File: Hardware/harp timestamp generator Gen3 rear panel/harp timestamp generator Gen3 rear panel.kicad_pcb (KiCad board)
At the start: 2 copper layers, 133 x 35 mm, 7 parts

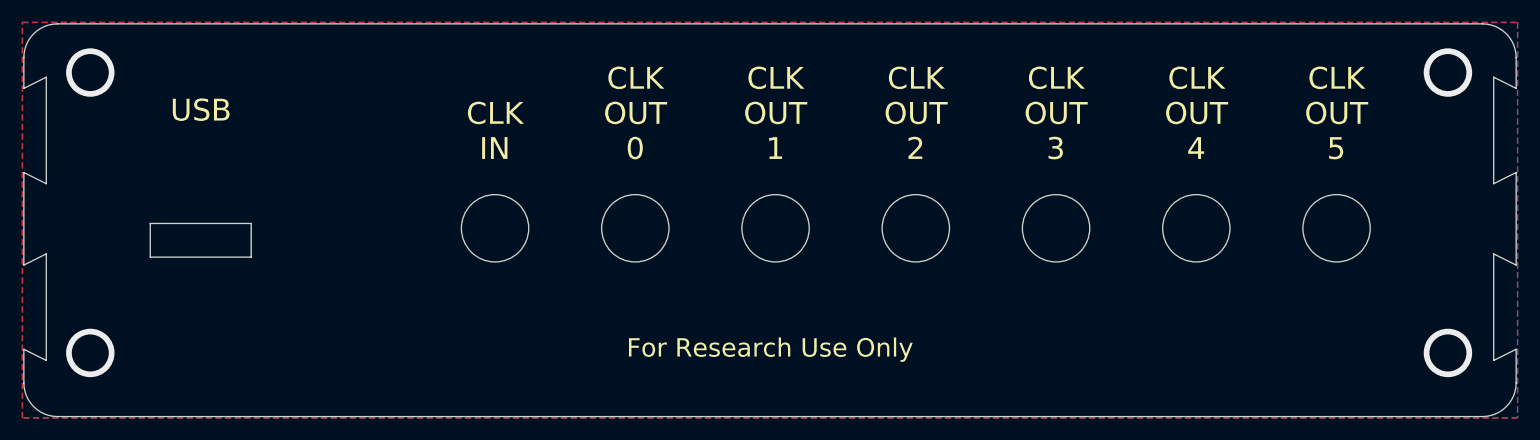
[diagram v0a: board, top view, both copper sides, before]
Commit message: review após 1ª produção de placas teste
> harp timestamp generator Gen3
  . mudança da case de Q2
  . mudança de ligação em 'Button0'

> harp timestamp generator Gen3 front panel
  . acerto no recorte da ficha IDC e interruptor bateria
  . modificação de setup no logo 'harp'

> harp timestamp generator Gen3 rear panel
  . acerto no recorte de ficha USB
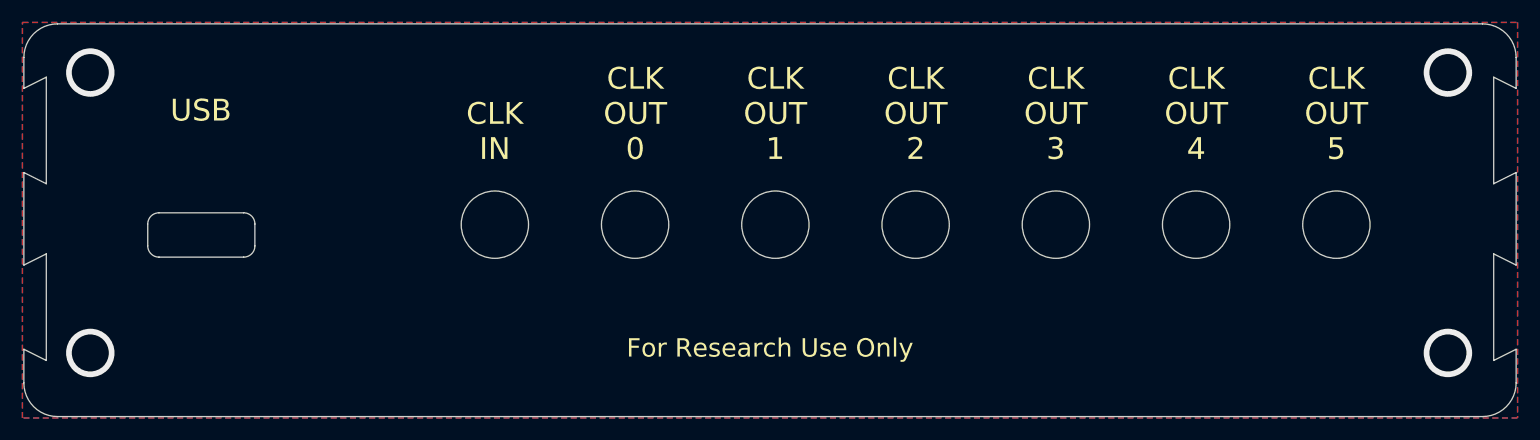
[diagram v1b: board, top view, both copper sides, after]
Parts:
- added REF**: Fiducial_Cross_1.5mm_Mask2mm, Fiducial:Fiducial_Cross_1.5mm_Mask2mm, F.Cu at (145.6, 109.0)
- moved UNK_HOLE_1 0.32 mm to (136.5, 105.4)
- moved UNK_HOLE_2 0.32 mm to (149.0, 105.4)
- moved UNK_HOLE_3 0.32 mm to (161.5, 105.4)
- moved UNK_HOLE_4 0.32 mm to (174.0, 105.4)
- moved UNK_HOLE_5 0.32 mm to (186.5, 105.4)
- moved UNK_HOLE_6 0.32 mm to (199.0, 105.4)
- moved UNK_HOLE_0 0.32 mm to (124.0, 105.4)
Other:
- outline, holes or cut-outs redrawn
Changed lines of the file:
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@@
 	(footprint "dummyfp6"
 		(layer "F.Cu")
-		(at 198.9975 105.7236)
+		(at 198.98 105.4)
 		(property "Reference" "UNK_HOLE_6"
 			(at 0 0 0)
@@
 	(footprint "dummyfp1"
 		(layer "F.Cu")
-		(at 136.4975 105.7236)
+		(at 136.48 105.4)
 		(property "Reference" "UNK_HOLE_1"
 			(at 0 0 0)
@@
 		(embedded_fonts no)
 	)
+	(footprint "Fiducial:Fiducial_Cross_1.5mm_Mask2mm"
+		(layer "F.Cu")
+		(at 145.6 109.05)
+		(descr "Fiducial, cross variant, 1.5mm bare copper, 2mm soldermask opening")
+		(tags "fiducial")
+		(property "Reference" "REF**"
+			(at 0 -1.95 0)
+			(layer "F.SilkS")
+			(hide yes)
+			(effects
+				(font
+					(size 1 1)
+					(thickness 0.15)
+				)
+			)
+		)
+		(property "Value" "Fiducial_Cross_1.5mm_Mask2mm"
+			(at 0 1.95 0)
+			(layer "F.Fab")
+			(hide yes)
+			(effects
+				(font
+					(size 1 1)
+					(thickness 0.15)
+				)
+			)
+		)
+		(property "Datasheet" ""
+			(at 0 0 0)
+			(layer "F.Fab")
+			(hide yes)
+			(effects
+				(font
+					(size 1.27 1.27)
+				)
+			)
+		)
+		(property "Description" ""
+			(at 0 0 0)
+			(layer "F.Fab")
+			(hide yes)
+			(effects
+				(font
+					(size 1.27 1.27)
+				)
+			)
+		)
+		(property "KiLib_Generator" "fiducial"
+			(at 0 0 0)
+			(layer "F.SilkS")
+			(hide yes)
+			(effects
+				(font
+					(size 1 1)
+					(thickness 0.15)
+				)
+			)
+		)
+		(attr smd board_only exclude_from_pos_files exclude_from_bom dnp)
+		(duplicate_pad_numbers_are_jumpers no)
+		(fp_circle
+			(center 0 0)
+			(end 1.25 0)
+			(stroke
+				(width 0.05)
+				(type solid)
+			)
+			(fill no)
+			(layer "F.CrtYd")
+		)
+		(embedded_fonts no)
+		(model "${KIPRJMOD}/harp timestamp generator.step"
+			(offset
+				(xyz 3 -0.75 -41.55)
+			)
+			(scale
+				(xyz 1 1 1)
+			)
+			(rotate
+				(xyz 90 -180 -0)
+			)
+		)
+	)
 	(footprint "dummyfp3"
 		(layer "F.Cu")
-		(at 161.4975 105.7236)
+		(at 161.48 105.4)
 		(property "Reference" "UNK_HOLE_3"
 			(at 0 0 0)
@@
 	(footprint "dummyfp4"
 		(layer "F.Cu")
-		(at 173.9975 105.7236)
+		(at 173.98 105.4)
 		(property "Reference" "UNK_HOLE_4"
 			(at 0 0 0)
@@
 	(footprint "dummyfp2"
 		(layer "F.Cu")
-		(at 148.9975 105.7236)
+		(at 148.98 105.4)
 		(property "Reference" "UNK_HOLE_2"
 			(at 0 0 0)
@@
 	(footprint "dummyfp0"
 		(layer "F.Cu")
-		(at 123.9975 105.7236)
+		(at 123.98 105.4)
 		(property "Reference" "UNK_HOLE_0"
 			(at 0 0 0)
@@
 	(footprint "dummyfp5"
 		(layer "F.Cu")
-		(at 186.4975 105.7236)
+		(at 186.48 105.4)
 		(property "Reference" "UNK_HOLE_5"
 			(at 0 0 0)
@@
 		(layer "Edge.Cuts")
 	)
-	(gr_rect
-		(start 93.2661 105.2936)
-		(end 102.2661 108.2936)
-		(radius 0.6)
-		(stroke
-			(width 0.1)
-			(type solid)
-		)
-		(fill no)
+	(gr_arc
+		(start 93.042893 105.342893)
+		(mid 93.335786 104.635786)
+		(end 94.042893 104.342893)
+		(stroke
+			(width 0.05)
+			(type default)
+		)
+		(layer "Edge.Cuts")
+	)
+	(gr_line
+		(start 93.042893 107.292893)
+		(end 93.042893 105.342893)
+		(stroke
+			(width 0.05)
+			(type solid)
+		)
+		(layer "Edge.Cuts")
+	)
+	(gr_line
+		(start 94.042893 104.342893)
+		(end 101.592893 104.342893)
+		(stroke
+			(width 0.05)
+			(type solid)
+		)
+		(layer "Edge.Cuts")
+	)
+	(gr_arc
+		(start 94.042893 108.292893)
+		(mid 93.335786 108)
+		(end 93.042893 107.292893)
+		(stroke
+			(width 0.05)
+			(type default)
+		)
+		(layer "Edge.Cuts")
+	)
+	(gr_line
+		(start 94.042893 108.292893)
+		(end 101.592893 108.292893)
+		(stroke
+			(width 0.05)
+			(type solid)
+		)
+		(layer "Edge.Cuts")
+	)
+	(gr_arc
+		(start 101.592893 104.342893)
+		(mid 102.3 104.635786)
+		(end 102.592893 105.342893)
+		(stroke
+			(width 0.05)
+			(type default)
+		)
+		(layer "Edge.Cuts")
+	)
+	(gr_arc
+		(start 102.592893 107.292893)
+		(mid 102.3 108)
+		(end 101.592893 108.292893)
+		(stroke
+			(width 0.05)
+			(type default)
+		)
+		(layer "Edge.Cuts")
+	)
+	(gr_line
+		(start 102.592893 107.292893)
+		(end 102.592893 105.342893)
+		(stroke
+			(width 0.05)
+			(type solid)
+		)
 		(layer "Edge.Cuts")
 	)
@@
 		)
 	)
+	(dimension
+		(type orthogonal)
+		(layer "User.2")
+		(pts
+			(xy 212.0011 122.5036) (xy 212.0011 87.5036)
+		)
+		(height 17.6489)
+		(orientation 1)
+		(format
+			(prefix "")
+			(suffix "")
+			(units 3)
+			(units_format 0)
+			(precision 2)
+		)
+		(style
+			(thickness 0.1)
+			(arrow_length 1.27)
+			(text_position_mode 0)
+			(arrow_direction outward)
+			(extension_height 0.58642)
+			(extension_offset 0.5)
+			(keep_text_aligned yes)
+		)
+		(gr_text "35.00"
+			(at 228.5 105.0036 90)
+			(layer "User.2")
+			(effects
+				(font
+					(size 1 1)
+					(thickness 0.15)
+				)
+			)
+		)
+	)
 	(via
 		(at 87.9221 116.8336)
@@
 		(drill 3.3)
 		(layers "F.Cu" "B.Cu")
+		(locked yes)
 		(net "GND")
 	)
@@
 		(drill 3.3)
 		(layers "F.Cu" "B.Cu")
+		(locked yes)
 		(net "GND")
 	)
@@
 		(drill 3.3)
 		(layers "F.Cu" "B.Cu")
+		(locked yes)
 		(net "GND")
 	)
@@
 		(drill 3.3)
 		(layers "F.Cu" "B.Cu")
+		(locked yes)
 		(net "GND")
 	)
@@
 		)
 	)
+	(group ""
+		(members "0643406a-888c-4944-bf51-0a0cd0e89263" "1e793d71-1e94-4e4e-a609-6d8bc9b89011"
+			"38a5300f-db5b-423a-bbc0-bfdac0bf9eb1" "4cf00b2a-7704-443f-83d4-288d28c30887"
+			"9b6a8fb4-b613-4542-a19f-ff99516b31b0" "ad647369-bc08-46c6-9336-e1bad566f79c"
+			"f622935f-7573-41a9-9361-ebca37b4e445"
+		)
+	)
+	(group ""
+		(members "3467fe31-29ec-4e3d-9eb5-4a56a8728343" "4080239d-c03a-43a9-8f6b-841bcd6cf368"
+			"415314f5-8784-47c5-a261-64f990d81beb" "9d611add-74a3-4437-94e7-4b3305d86c51"
+			"ac99ed75-1616-4d85-ae6b-53e6533ea19c" "ca4b64b7-6551-46ab-b10c-9f1666c3940d"
+			"cb814115-3cea-4240-963e-56d6f7f476c8" "d6f09a21-9cbb-4821-b171-c207cda2719d"
+		)
+	)
